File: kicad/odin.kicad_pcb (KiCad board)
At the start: 8 copper layers, 100 x 100 mm, 553 parts, among them J1 USB-C, J19 2.54-2*3P, J2 FPGA JTAG, J20 2.54-2*3P, J3 WingTAT 2044-2X32G00SA, J5 WingTAT 2044-2X32G00SA, J50 9-21V POWER IN, J51 CTRL SWD, J52 PZ254V-11-02P, J53 XFCN PM254V-11-07-H85, J54 XFCN PM254V-11-07-H85, J55 XFCN PM254V-11-07-H85, J56 XFCN PM254V-11-07-H85, J57 XFCN PM254V-11-07-H85, J58 XFCN PM254V-11-07-H85, J62 XFCN PM254V-11-07-H85, J63 XFCN PM254V-11-07-H85, J64 XFCN PM254V-11-07-H85, J65 XFCN PM254V-11-07-H85, J68 AUX IN 9-28V UNREGULATED, J7 PM254-2-08-Z-8.5, J70 ETH, J71 LINK P, J72 LINK Q, J73 HDMI OUT, J74 microSD, J8 PM254-2-08-Z-8.5, Q3 BSS138LT1G, Q4 BSS138LT1G, Q6 BSS138LT1G, Q7 BSS138LT1G, SW1 CTRL BOOT, U1 XC7A100T-2FGG676I, U10 SN74LXC8T245PWR, U11 AP63300WU-7, U12 AP63300WU-7, U13 TLV62569DRLR, U14 TLV62569DRLR, U15 SY8047QDC, U16 TLV62569DRLR, U17 PCF8574T_3,518, U18 CH224K, U2 APS6404L-SQN-SN, U20 SN74CB3Q3384APWR, U21 TPS22950CDDCR, U22 TPS22950CDDCR, U23 TPS22953DSQR, U24 TPS22953DSQR, U26 TPS259470ARPWR, U3 APS6404L-SQN-SN, U30 RTL8211FD-CG, U31 TPD12S016PWR, U32 W9825G6KH-6, U33 MR25H10CDF, U34 TPS2121RUXR, U4 APS6404L-SQN-SN, U5 APS6404L-SQN-SN, U6 W25Q256JVEIQ, U7 RP2350B, U8 W25Q32JVZP, U9 SN74LXC8T245PWR, X3 25MHz 12pF, X4 50MHz CMOS, Y1 12MHz ABM8-272-T3

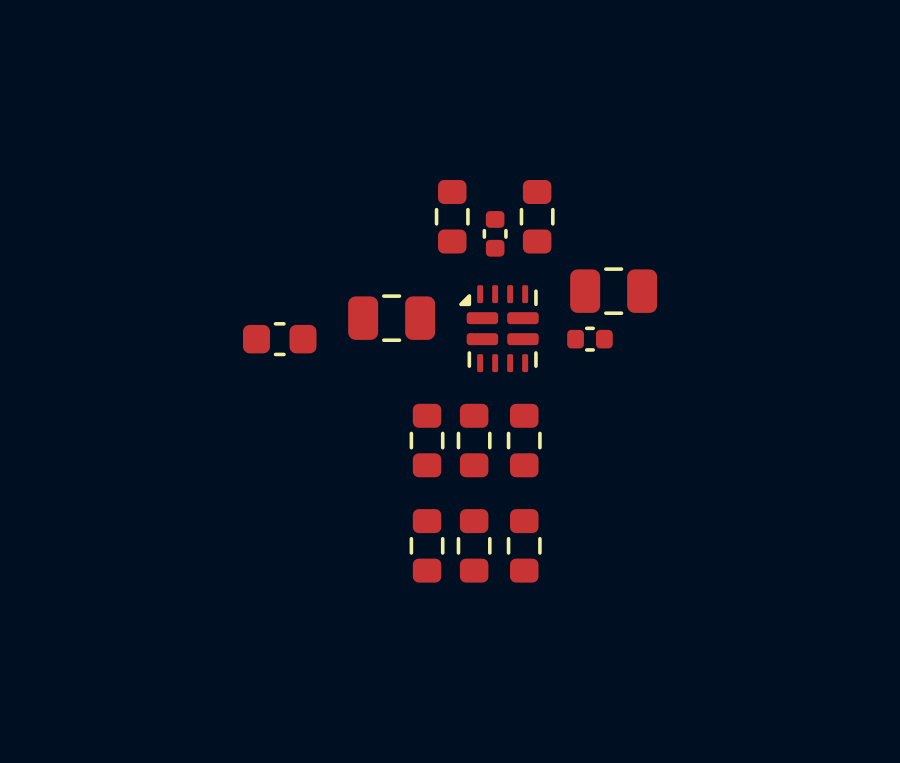
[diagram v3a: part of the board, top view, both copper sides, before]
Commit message: Island U34 re-applied: IN2 bypass innermost at pin 2 (profile rule)
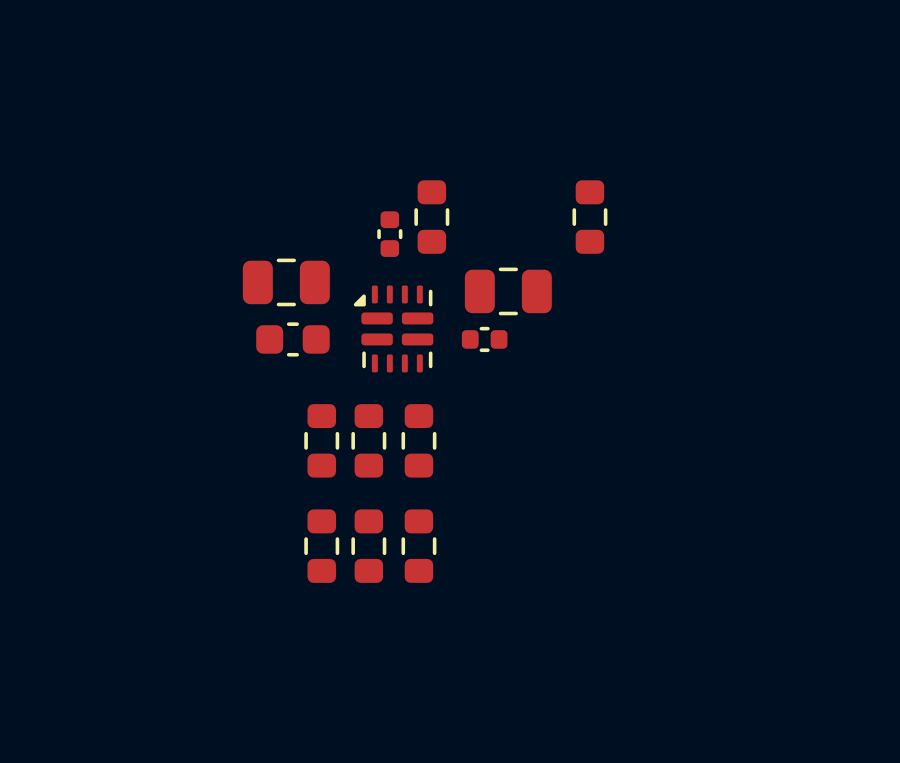
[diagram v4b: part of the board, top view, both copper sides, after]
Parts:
- moved R169 4.59 mm to (443.4, 44.1)
- moved C266 3.71 mm to (433.2, 46.3)
- moved C264 3.51 mm to (439.8, 48.2)
- moved R162 3.51 mm to (437.6, 51.6)
- moved R163 3.51 mm to (437.6, 55.1)
- moved C263 3.51 mm to (436.7, 44.7)
- moved C265 3.51 mm to (440.6, 46.6)
- moved R164 3.51 mm to (436.0, 51.6)
- moved R165 3.51 mm to (436.0, 55.1)
- moved R166 3.51 mm to (434.4, 51.6)
- moved R167 3.51 mm to (434.4, 55.1)
- moved R168 3.51 mm to (438.1, 44.1)
- moved U34 3.51 mm to (436.9, 47.9)
- moved C280 0.44 mm to (433.4, 48.2)
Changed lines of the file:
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@@
 	(footprint "Resistor_SMD:R_0603_1608Metric"
 		(layer "F.Cu")
-		(at 441.16 51.6 90)
+		(at 437.65 51.61 90)
 		(descr "100k resistor from VBUS5_PR1 to VBUS, for U34 (+5V source mux): U34 priority sense: VBUS wins above 4.44 V (PR1 above CP2) unless Q6 (9 V request) or Q7 (screw input present) holds it at ground")
 		(tags "resistor")
@@
 	(footprint "Package_DFN_QFN:Texas_VQFN-HR-12_2x2.5mm_P0.5mm"
 		(layer "F.Cu")
-		(at 440.44 47.87)
+		(at 436.93 47.88)
 		(descr "+5V source mux: TI TPS2121 power mux: passes plain 5 V USB straight to the +5V rail; hands the rail to U11 while the board controller asks for 9 V (Q6), while the screw input is powered (Q7), or if VBUS goes above about 5.6 V or away. Blocks reverse current both ways, limits to about 2.5 A.")
 		(tags "RUX0012A Texas VQFN-HR NoLead")
@@
 	(footprint "Capacitor_SMD:C_0805_2012Metric"
 		(layer "F.Cu")
-		(at 436.74 47.52 180)
+		(at 433.23 46.33 180)
 		(descr "22uF bypass on +5V, for U34 (+5V source mux)")
 		(tags "capacitor")
@@
 	(footprint "Capacitor_SMD:C_0402_1005Metric"
 		(layer "F.Cu")
-		(at 440.19 44.71 90)
+		(at 436.68 44.72 90)
 		(descr "100nF capacitor from VBUS5_SS to GND, for U34 (+5V source mux): sets how fast U34 ramps the +5V rail, about 780 V/s")
 		(tags "capacitor")
@@
 	(footprint "Resistor_SMD:R_0603_1608Metric"
 		(layer "F.Cu")
-		(at 441.59 44.14 90)
+		(at 438.08 44.15 90)
 		(descr "44.2k resistor from VBUS5_ILIM to GND, for U34 (+5V source mux): sets U34's current limit, about 2.5 A")
 		(tags "resistor")
@@
 	(footprint "Resistor_SMD:R_0603_1608Metric"
 		(layer "F.Cu")
-		(at 438.76 44.14 -90)
+		(at 443.35 44.15 -90)
 		(descr "10k resistor from VBUS5_ST to +3V3, for U7 (board controller): U34 status to the board controller: low when U11 feeds +5V")
 		(tags "resistor")
@@
 	(footprint "Resistor_SMD:R_0603_1608Metric"
 		(layer "F.Cu")
-		(at 441.16 55.11 -90)
+		(at 437.65 55.12 -90)
 		(descr "36.5k resistor from VBUS5_PR1 to GND, for U34 (+5V source mux): U34 priority sense: VBUS wins above 4.44 V (PR1 above CP2) unless Q6 (9 V request) or Q7 (screw input present) holds it at ground")
 		(tags "resistor")
@@
 	(footprint "Capacitor_SMD:C_0805_2012Metric"
 		(layer "F.Cu")
-		(at 444.14 46.62)
+		(at 440.63 46.63)
 		(descr "22uF bypass on +5V, for U34 (+5V source mux)")
 		(tags "capacitor")
@@
 	(footprint "Resistor_SMD:R_0603_1608Metric"
 		(layer "F.Cu")
-		(at 437.92 55.11 -90)
+		(at 434.41 55.12 -90)
 		(descr "56.2k resistor from VBUS5_CP2 to GND, for U34 (+5V source mux): U34 comparison level, 1.19 V from +3V3; enables the 5 us switchover")
 		(tags "resistor")
@@
 	(footprint "Resistor_SMD:R_0603_1608Metric"
 		(layer "F.Cu")
-		(at 439.49 51.6 90)
+		(at 435.98 51.61 90)
 		(descr "100k resistor from VBUS5_OV1 to VBUS, for U34 (+5V source mux): U34 VBUS overvoltage backstop: VBUS is dropped above 5.3-5.9 V (5.63 V typical) if a source raises it unasked")
 		(tags "resistor")
@@
 	(footprint "Resistor_SMD:R_0603_1608Metric"
 		(layer "F.Cu")
-		(at 439.49 55.11 -90)
+		(at 435.98 55.12 -90)
 		(descr "23.2k resistor from VBUS5_OV1 to GND, for U34 (+5V source mux): U34 VBUS overvoltage backstop: VBUS is dropped above 5.3-5.9 V (5.63 V typical) if a source raises it unasked")
 		(tags "resistor")
@@
 	(footprint "Capacitor_SMD:C_0402_1005Metric"
 		(layer "F.Cu")
-		(at 443.35 48.22)
+		(at 439.84 48.23)
 		(descr "100nF 25V bypass on VBUS, for U34 (+5V source mux)")
 		(tags "capacitor")
@@
 	(footprint "Resistor_SMD:R_0603_1608Metric"
 		(layer "F.Cu")
-		(at 437.92 51.6 90)
+		(at 434.41 51.61 90)
 		(descr "100k resistor from VBUS5_CP2 to +3V3, for U34 (+5V source mux): U34 comparison level, 1.19 V from +3V3; enables the 5 us switchover")
 		(tags "resistor")
@@
 	(footprint "Capacitor_SMD:C_0603_1608Metric"
 		(layer "F.Cu")
-		(at 433.01 48.22 180)
+		(at 433.45 48.23 180)
 		(descr "1uF bypass on +5V_BUCK, for U34 (+5V source mux)")
 		(tags "capacitor")
@@
 	)
 	(gr_rect
-		(start 430.005 41.135)
-		(end 447.365 58.115)
+		(start 430.005 41.145)
+		(end 445.605 58.125)
 		(stroke
 			(width 0.15)
@@
 	)
 	(gr_rect
-		(start 430.005 35.995)
-		(end 447.365 41.135)
+		(start 430.005 36.005)
+		(end 445.605 41.145)
 		(stroke
 			(width 0.15)
@@
 	)
 	(gr_text "island U34"
-		(at 430.405 37.595 0)
+		(at 430.405 37.605 0)
 		(layer "Cmts.User")
 		(effects
@@
 	)
 	(gr_text "+5V source mux\nTPS2121, 14 parts,\n2026-10-29"
-		(at 430.405 37.895 0)
+		(at 430.405 37.905 0)
 		(layer "Cmts.User")
 		(effects
@@
 	(group "island U34"
 		(members
-			"35deaf51-a170-4e1a-9ef6-d068fa9181ed"
-			"8369e237-ea62-4907-a6a0-54b78e98bf71"
-			"0596f1c4-8e6c-4502-afe7-404ebe20fb43"
-			"c245fbf2-7c0c-4847-baaa-8121932f2aab"
+			"2fda848b-5527-4b65-a311-194a488b7f32"
+			"099504d1-affd-4028-9047-2978fa6f1885"
+			"6192a37a-0662-4e67-95c3-599803e18322"
+			"1f70a80a-2b33-4501-ba19-915476d41118"
 			"13ecfdc8-8b61-4334-810e-42b36423c172"
 			"1aca21b5-7d8e-4b4f-9384-0ba20e24a880"

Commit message: Island J57 re-applied: PIN V fuse and bulk capacitor inboard, clear of the key post
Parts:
- moved C144 295.4 mm to (436.2, 67.9)
- moved F2 295.4 mm to (443.8, 67.5)
- moved F3 295.4 mm to (439.4, 67.5)
- moved F1 294.2 mm to (434.7, 73.6), turned to 90 degrees
- moved F4 292.5 mm to (447.3, 74.8)
- moved J57 292.5 mm to (440.7, 69.8)
- moved C143 292.3 mm to (432.5, 73.3), turned to -90 degrees
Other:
- board text added: "slot L power socket XFCN PM254V-11-07, 7 parts, 2026-10-29"
- board text removed: "slot L power socket XFCN PM254V-11-07, 7 parts, 2026-10-28 + MK76"
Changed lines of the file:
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@@
 	(footprint "EasyEDA:HDR-TH_7P-P2.54-V-F"
 		(layer "F.Cu")
-		(at 732.06 44.31)
+		(at 440.67 69.79)
 		(descr "slot L power socket: 1x7 female socket: PIN V, 3.3 V, 5 V and AUX for the extension, each beside a ground.")
 		(property "Reference" "J57"
@@
 	(footprint "odin:Fuse_TECHFUSE_SMD2018"
 		(layer "F.Cu")
-		(at 738.65 49.31 90)
+		(at 447.26 74.79 90)
 		(descr "1.1A 33V resettable fuse feeding SLOT_L_AUX from AUX_RAIL, for J57 (slot L power socket)")
 		(tags "PTC 2018 5045metric")
@@
 	(footprint "EasyEDA:F1206"
 		(layer "F.Cu")
-		(at 738.14 42.02 180)
+		(at 443.84 67.5 180)
 		(descr "500mA resettable fuse feeding SLOT_L_5V from +5V_EXT, for J57 (slot L power socket)")
 		(property "Reference" "F2"
@@
 	(footprint "EasyEDA:F1206"
 		(layer "F.Cu")
-		(at 733.75 42.02 180)
+		(at 439.45 67.5 180)
 		(descr "300mA resettable fuse feeding SLOT_L_3V3 from +3V3_EXT, for J57 (slot L power socket)")
 		(property "Reference" "F3"
@@
 	(footprint "Capacitor_SMD:C_0805_2012Metric"
 		(layer "F.Cu")
-		(at 723.12 41.88)
+		(at 432.51 73.29 -90)
 		(descr "10uF bypass on SLOT_L_PIN_VOLTAGE, for J57 (slot L power socket)")
 		(tags "capacitor")
 		(property "Reference" "C143"
-			(at 0 -1.68 0)
+			(at 0 -1.68 270)
 			(layer "F.Fab")
 			(effects
@@
 		)
 		(property "Value" "10uF"
-			(at 0 1.68 0)
+			(at 0 1.68 270)
 			(layer "F.Fab")
 			(effects
@@
 		)
 		(property "Datasheet" ""
-			(at 0 0 0)
+			(at 0 0 270)
 			(layer "F.Fab")
 			(hide yes)
@@
 		)
 		(property "Description" "10uF bypass on SLOT_L_PIN_VOLTAGE, for J57 (slot L power socket)"
-			(at 0 0 0)
+			(at 0 0 270)
 			(layer "F.Fab")
 			(hide yes)
@@
 		)
 		(property "LCSC Part" "C15850"
-			(at 0 0 0)
+			(at 0 0 270)
 			(layer "F.SilkS")
 			(hide yes)
@@
 		)
 		(fp_text user "${REFERENCE}"
-			(at 0 0 0)
+			(at 0 0 270)
 			(layer "F.Fab")
 			(effects
@@
 		)
 		(pad "1" smd roundrect
-			(at -0.95 0)
+			(at -0.95 0 270)
 			(size 1 1.45)
 			(layers "F.Cu" "F.Mask" "F.Paste")
@@
 		)
 		(pad "2" smd roundrect
-			(at 0.95 0)
+			(at 0.95 0 270)
 			(size 1 1.45)
 			(layers "F.Cu" "F.Mask" "F.Paste")
@@
 	(footprint "EasyEDA:F1206"
 		(layer "F.Cu")
-		(at 727.19 42.02 180)
+		(at 434.68 73.61 90)
 		(descr "500mA resettable fuse feeding SLOT_L_PIN_VOLTAGE from +3V3_EXT, for J57 (slot L power socket)")
 		(property "Reference" "F1"
-			(at 0 -4 180)
+			(at 0 -4 90)
 			(layer "F.Fab")
 			(effects
@@
 		)
 		(property "Value" "500mA"
-			(at 0 4 180)
+			(at 0 4 90)
 			(layer "F.Fab")
 			(effects
@@
 		)
 		(property "Datasheet" ""
-			(at 0 0 180)
+			(at 0 0 90)
 			(layer "F.Fab")
 			(hide yes)
@@
 		)
 		(property "Description" "500mA resettable fuse feeding SLOT_L_PIN_VOLTAGE from +3V3_EXT, for J57 (slot L power socket)"
-			(at 0 0 180)
+			(at 0 0 90)
 			(layer "F.Fab")
 			(hide yes)
@@
 		)
 		(property "LCSC Part" "C269115"
-			(at 0 0 0)
+			(at 0 0 270)
 			(layer "F.SilkS")
 			(hide yes)
@@
 		)
 		(fp_text user "${REFERENCE}"
-			(at 0 0 180)
+			(at 0 0 90)
 			(layer "F.Fab")
 			(effects
@@
 		)
 		(pad "1" smd rect
-			(at -1.45 0 180)
+			(at -1.45 0 90)
 			(size 1.19 1.728)
 			(layers "F.Cu" "F.Mask" "F.Paste")
@@
 		)
 		(pad "2" smd rect
-			(at 1.45 0 180)
+			(at 1.45 0 90)
 			(size 1.19 1.728)
 			(layers "F.Cu" "F.Mask" "F.Paste")
@@
 	(footprint "Capacitor_SMD:C_0402_1005Metric"
 		(layer "F.Cu")
-		(at 730.47 42.4)
+		(at 436.17 67.88)
 		(descr "100nF bypass on SLOT_L_3V3, for J57 (slot L power socket)")
 		(tags "capacitor")
@@
 	)
 	(gr_rect
-		(start 718.855 34.235)
-		(end 742.725 39.375)
-		(stroke
-			(width 0.15)
-			(type solid)
-		)
-		(fill no)
-		(layer "Cmts.User")
-	)
-	(gr_rect
-		(start 718.855 39.375)
-		(end 742.725 54.035)
-		(stroke
-			(width 0.15)
-			(type dash)
-		)
-		(fill no)
-		(layer "Cmts.User")
-	)
-	(gr_rect
 		(start 720.175 20.995)
 		(end 743.945 25.155)
@@
 		)
 	)
-	(gr_text "slot L power socket\nXFCN PM254V-11-07, 7 parts, 2026-10-28\n+ MK76"
-		(at 719.255 36.135 0)
-		(layer "Cmts.User")
-		(effects
-			(font
-				(size 0.7 0.7)
-				(thickness 0.105)
-			)
-			(justify left top)
-		)
-	)
 	(gr_text "slot L signal socket\ngeneric, 1 parts, 2026-10-28"
 		(at 720.575 22.895 0)
@@
 		)
 	)
-	(gr_text "island J57"
-		(at 719.255 35.835 0)
-		(layer "Cmts.User")
-		(effects
-			(font
-				(size 1.2 1.2)
-				(thickness 0.18)
-			)
-			(justify left bottom)
-		)
-	)
 	(gr_text "island J7"
 		(at 720.575 22.595 0)
@@
 		)
 	)
-	(group "island J57"
-		(members "39f26566-f6a8-4d4c-8153-3c027c047d21" "3b958773-f2b2-4769-956a-30ba41cca38c"
-			"3bcba273-b3d2-489b-8106-857d26a6e446" "446ff4e5-71a0-4bd5-8a83-5fe5be824c70"
-			"44b8b4da-3d00-4912-afe2-adb9487becb4" "641a270c-ae03-4bc7-adf6-dd1b1ab16ad4"
-			"9c04bdd4-e0f1-4584-a31d-5dcc5e22e03f" "b3a7c832-95d4-4a51-a6d2-8346b7025bcb"
-			"b593930b-5d1d-4099-a8f5-28a19cffbeba" "b8509478-2847-4911-8a3f-4b9eda65c405"
-			"e4e735e8-1ada-410a-81ec-c52243090903" "f479abd2-7b8c-48cb-80cd-49ca92ddee8d"
-		)
-	)
 	(group "island U13"
 		(members "08348b48-d6ef-47ea-b841-61e06e7f39f0" "0df03976-d041-4e34-a6e0-d9eea2be3f3e"
@@
 		)
 	)
+	(gr_rect
+		(start 430.005 65.136)
+		(end 451.335 79.515)
+		(stroke
+			(width 0.15)
+			(type dash)
+		)
+		(fill no)
+		(layer "Cmts.User")
+	)
+	(gr_rect
+		(start 430.005 59.996)
+		(end 451.335 65.136)
+		(stroke
+			(width 0.15)
+			(type solid)
+		)
+		(fill no)
+		(layer "Cmts.User")
+	)
+	(gr_text "island J57"
+		(at 430.405 61.596 0)
+		(layer "Cmts.User")
+		(effects
+			(font
+				(size 1.2 1.2)
+				(thickness 0.18)
+			)
+			(justify left bottom)
+		)
+	)
+	(gr_text "slot L power socket\nXFCN PM254V-11-07, 7 parts,\n2026-10-29"
+		(at 430.405 61.896 0)
+		(layer "Cmts.User")
+		(effects
+			(font
+				(size 0.7 0.7)
+				(thickness 0.105)
+			)
+			(justify left top)
+		)
+	)
+	(group "island J57"
+		(members
+			"ba1f36c3-52d9-4b6c-a10e-4c081cf01d9b"
+			"4011c184-c2ab-4fe7-b39f-1efd5085c810"
+			"e2777917-bcb7-443b-a494-0bed06a3a704"
+			"c6fbe6dc-cb88-46fa-affb-89f2c61cd4cb"
+			"39f26566-f6a8-4d4c-8153-3c027c047d21"
+			"b593930b-5d1d-4099-a8f5-28a19cffbeba"
+			"f479abd2-7b8c-48cb-80cd-49ca92ddee8d"
+			"b8509478-2847-4911-8a3f-4b9eda65c405"
+			"44b8b4da-3d00-4912-afe2-adb9487becb4"
+			"9c04bdd4-e0f1-4584-a31d-5dcc5e22e03f"
+			"3bcba273-b3d2-489b-8106-857d26a6e446"
+		)
+	)

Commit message: Island J58 re-applied: PIN V fuse and bulk capacitor inboard, clear of the key post
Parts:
- moved C146 353.3 mm to (436.2, 88.9)
- moved F6 353.3 mm to (443.8, 88.5)
- moved F7 353.3 mm to (439.4, 88.5)
- moved F5 352.3 mm to (434.7, 94.6), turned to 90 degrees
- moved C145 350.4 mm to (432.5, 94.3), turned to -90 degrees
- moved J58 350.4 mm to (440.7, 90.8)
- moved F8 350.4 mm to (447.2, 95.8)
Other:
- board text added: "slot M power socket XFCN PM254V-11-07, 7 parts, 2026-10-29"
- board text removed: "slot M power socket XFCN PM254V-11-07, 7 parts, 2026-10-28 + MK77"
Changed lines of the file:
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@@
 	(footprint "Capacitor_SMD:C_0402_1005Metric"
 		(layer "F.Cu")
-		(at 786.35 42.4)
+		(at 436.16 88.88)
 		(descr "100nF bypass on SLOT_M_3V3, for J58 (slot M power socket)")
 		(tags "capacitor")
@@
 	(footprint "EasyEDA:HDR-TH_7P-P2.54-V-F"
 		(layer "F.Cu")
-		(at 787.94 44.31)
+		(at 440.66 90.79)
 		(descr "slot M power socket: 1x7 female socket: PIN V, 3.3 V, 5 V and AUX for the extension, each beside a ground.")
 		(property "Reference" "J58"
@@
 	(footprint "Capacitor_SMD:C_0805_2012Metric"
 		(layer "F.Cu")
-		(at 779 41.88)
+		(at 432.5 94.29 -90)
 		(descr "10uF bypass on SLOT_M_PIN_VOLTAGE, for J58 (slot M power socket)")
 		(tags "capacitor")
 		(property "Reference" "C145"
-			(at 0 -1.68 0)
+			(at 0 -1.68 270)
 			(layer "F.Fab")
 			(effects
@@
 		)
 		(property "Value" "10uF"
-			(at 0 1.68 0)
+			(at 0 1.68 270)
 			(layer "F.Fab")
 			(effects
@@
 		)
 		(property "Datasheet" ""
-			(at 0 0 0)
+			(at 0 0 270)
 			(layer "F.Fab")
 			(hide yes)
@@
 		)
 		(property "Description" "10uF bypass on SLOT_M_PIN_VOLTAGE, for J58 (slot M power socket)"
-			(at 0 0 0)
+			(at 0 0 270)
 			(layer "F.Fab")
 			(hide yes)
@@
 		)
 		(property "LCSC Part" "C15850"
-			(at 0 0 0)
+			(at 0 0 270)
 			(layer "F.SilkS")
 			(hide yes)
@@
 		)
 		(fp_text user "${REFERENCE}"
-			(at 0 0 0)
+			(at 0 0 270)
 			(layer "F.Fab")
 			(effects
@@
 		)
 		(pad "1" smd roundrect
-			(at -0.95 0)
+			(at -0.95 0 270)
 			(size 1 1.45)
 			(layers "F.Cu" "F.Mask" "F.Paste")
@@
 		)
 		(pad "2" smd roundrect
-			(at 0.95 0)
+			(at 0.95 0 270)
 			(size 1 1.45)
 			(layers "F.Cu" "F.Mask" "F.Paste")
@@
 	(footprint "EasyEDA:F1206"
 		(layer "F.Cu")
-		(at 794.02 42.02 180)
+		(at 443.83 88.5 180)
 		(descr "500mA resettable fuse feeding SLOT_M_5V from +5V_EXT, for J58 (slot M power socket)")
 		(property "Reference" "F6"
@@
 	(footprint "EasyEDA:F1206"
 		(layer "F.Cu")
-		(at 783.07 42.02 180)
+		(at 434.67 94.61 90)
 		(descr "500mA resettable fuse feeding SLOT_M_PIN_VOLTAGE from +3V3_EXT, for J58 (slot M power socket)")
 		(property "Reference" "F5"
-			(at 0 -4 180)
+			(at 0 -4 90)
 			(layer "F.Fab")
 			(effects
@@
 		)
 		(property "Value" "500mA"
-			(at 0 4 180)
+			(at 0 4 90)
 			(layer "F.Fab")
 			(effects
@@
 		)
 		(property "Datasheet" ""
-			(at 0 0 180)
+			(at 0 0 90)
 			(layer "F.Fab")
 			(hide yes)
@@
 		)
 		(property "Description" "500mA resettable fuse feeding SLOT_M_PIN_VOLTAGE from +3V3_EXT, for J58 (slot M power socket)"
-			(at 0 0 180)
+			(at 0 0 90)
 			(layer "F.Fab")
 			(hide yes)
@@
 		)
 		(property "LCSC Part" "C269115"
-			(at 0 0 0)
+			(at 0 0 270)
 			(layer "F.SilkS")
 			(hide yes)
@@
 		)
 		(fp_text user "${REFERENCE}"
-			(at 0 0 180)
+			(at 0 0 90)
 			(layer "F.Fab")
 			(effects
@@
 		)
 		(pad "1" smd rect
-			(at -1.45 0 180)
+			(at -1.45 0 90)
 			(size 1.19 1.728)
 			(layers "F.Cu" "F.Mask" "F.Paste")
@@
 		)
 		(pad "2" smd rect
-			(at 1.45 0 180)
+			(at 1.45 0 90)
 			(size 1.19 1.728)
 			(layers "F.Cu" "F.Mask" "F.Paste")
@@
 	(footprint "odin:Fuse_TECHFUSE_SMD2018"
 		(layer "F.Cu")
-		(at 794.53 49.31 90)
+		(at 447.25 95.79 90)
 		(descr "1.1A 33V resettable fuse feeding SLOT_M_AUX from AUX_RAIL, for J58 (slot M power socket)")
 		(tags "PTC 2018 5045metric")
@@
 	(footprint "EasyEDA:F1206"
 		(layer "F.Cu")
-		(at 789.63 42.02 180)
+		(at 439.44 88.5 180)
 		(descr "300mA resettable fuse feeding SLOT_M_3V3 from +3V3_EXT, for J58 (slot M power socket)")
 		(property "Reference" "F7"
@@
 	)
 	(gr_rect
-		(start 774.735 34.235)
-		(end 798.605 39.375)
-		(stroke
-			(width 0.15)
-			(type solid)
-		)
-		(fill no)
-		(layer "Cmts.User")
-	)
-	(gr_rect
-		(start 774.735 39.375)
-		(end 798.605 54.035)
-		(stroke
-			(width 0.15)
-			(type dash)
-		)
-		(fill no)
-		(layer "Cmts.User")
-	)
-	(gr_rect
 		(start 775.665 65.795)
 		(end 789.67 71.915)
@@
 		)
 	)
-	(gr_text "slot M power socket\nXFCN PM254V-11-07, 7 parts, 2026-10-28\n+ MK77"
-		(at 775.135 36.135 0)
-		(layer "Cmts.User")
-		(effects
-			(font
-				(size 0.7 0.7)
-				(thickness 0.105)
-			)
-			(justify left top)
-		)
-	)
 	(gr_text "1.8 V regulator,\nalways on\nTLV62569, 8 parts,\n2026-10-29"
 		(at 776.065 67.695 0)
@@
 		)
 	)
-	(gr_text "island J58"
-		(at 775.135 35.835 0)
-		(layer "Cmts.User")
-		(effects
-			(font
-				(size 1.2 1.2)
-				(thickness 0.18)
-			)
-			(justify left bottom)
-		)
-	)
 	(gr_text "island U14"
 		(at 776.065 67.395 0)
@@
 		)
 	)
-	(group "island J58"
-		(members "157a4ac4-7672-42a1-b9cf-3c5e0d6a6607" "3b46ecf0-b1b6-4614-89a7-f997c19bc35a"
-			"4103ffa7-d2c5-4187-b64a-33826d7d8fe3" "4be0b073-5183-49f6-8c94-4852acce0696"
-			"4fac1b6c-7f39-4384-b271-785f73b09363" "76c0d251-bd9b-4bf5-b5b5-8d62f072f928"
-			"82a6b1e5-a320-46f6-b4e4-fa684a80d6bd" "8977862b-8d80-4a86-8a52-4cc647745774"
-			"9e4298d7-e27e-4dfc-b926-3805b295719f" "a8f614d3-9ab7-4197-830c-cdc4ddc8fde4"
-			"d8e68604-36d9-4c97-8b1e-95c4fe23d73b" "ec7dd26a-bb94-4186-adfb-2992c6ddf8c1"
-		)
-	)
 	(group "island U16"
 		(members "1757b1c4-491c-48fb-809d-62eb3fef5cf5" "17fa6aba-c039-4e54-804e-99aa4caa5e85"
@@
 		)
 	)
+	(gr_rect
+		(start 429.995 86.136)
+		(end 451.325 100.515)
+		(stroke
+			(width 0.15)
+			(type dash)
+		)
+		(fill no)
+		(layer "Cmts.User")
+	)
+	(gr_rect
+		(start 429.995 80.996)
+		(end 451.325 86.136)
+		(stroke
+			(width 0.15)
+			(type solid)
+		)
+		(fill no)
+		(layer "Cmts.User")
+	)
+	(gr_text "island J58"
+		(at 430.395 82.596 0)
+		(layer "Cmts.User")
+		(effects
+			(font
+				(size 1.2 1.2)
+				(thickness 0.18)
+			)
+			(justify left bottom)
+		)
+	)
+	(gr_text "slot M power socket\nXFCN PM254V-11-07, 7 parts,\n2026-10-29"
+		(at 430.395 82.896 0)
+		(layer "Cmts.User")
+		(effects
+			(font
+				(size 0.7 0.7)
+				(thickness 0.105)
+			)
+			(justify left top)
+		)
+	)
+	(group "island J58"
+		(members
+			"7bfdba0d-d3f2-4551-98b6-e4db96983d35"
+			"db3c2224-6ad0-4dda-8792-e6b1e9d90c6f"
+			"61d4c9a2-7466-4590-94ad-da9768a11687"
+			"8902f35a-76e7-4ad5-9948-ca76f1345d3d"
+			"4fac1b6c-7f39-4384-b271-785f73b09363"
+			"76c0d251-bd9b-4bf5-b5b5-8d62f072f928"
+			"3b46ecf0-b1b6-4614-89a7-f997c19bc35a"
+			"8977862b-8d80-4a86-8a52-4cc647745774"
+			"82a6b1e5-a320-46f6-b4e4-fa684a80d6bd"
+			"d8e68604-36d9-4c97-8b1e-95c4fe23d73b"
+			"9e4298d7-e27e-4dfc-b926-3805b295719f"
+		)
+	)
